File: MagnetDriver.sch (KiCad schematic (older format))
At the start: 54 parts, among them J1 MAGNET1, J2 MAGNET2, J3 INPUT_JACK, J4 PWR_IN, Q1 2N3904, Q2 TIP122, Q3 TIP32A, Q4 2N3904, Q5 TIP122, Q6 TIP32A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

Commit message: checked schematic + footprints
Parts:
- C3, C6: value 0.1uf -> 470pf
- J3: footprint HammerheadAudio:Tayda_3.5mm_stereo_TRS_jack_A-853 -> HammerheadAudio:Tayda_SwitchedStereoJack-PJ-307
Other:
- moved on the sheet: C1, C10, C2, C3, C4, C5, C6, C7, C8, C9, D1, D2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

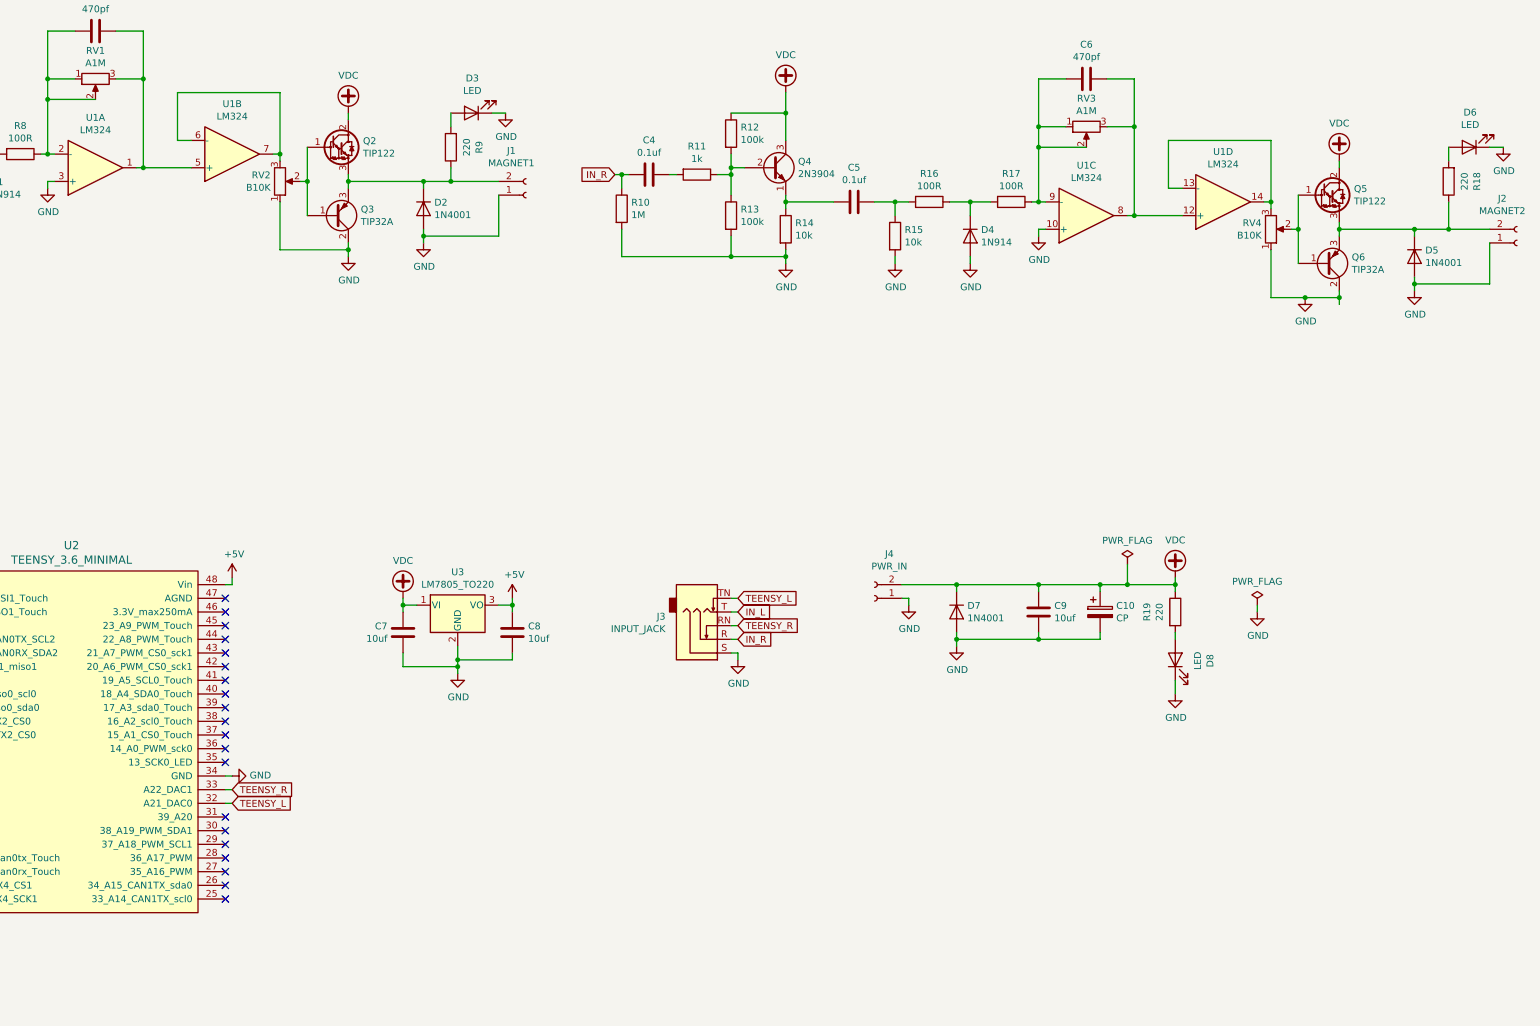
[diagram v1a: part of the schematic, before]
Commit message: arranging components
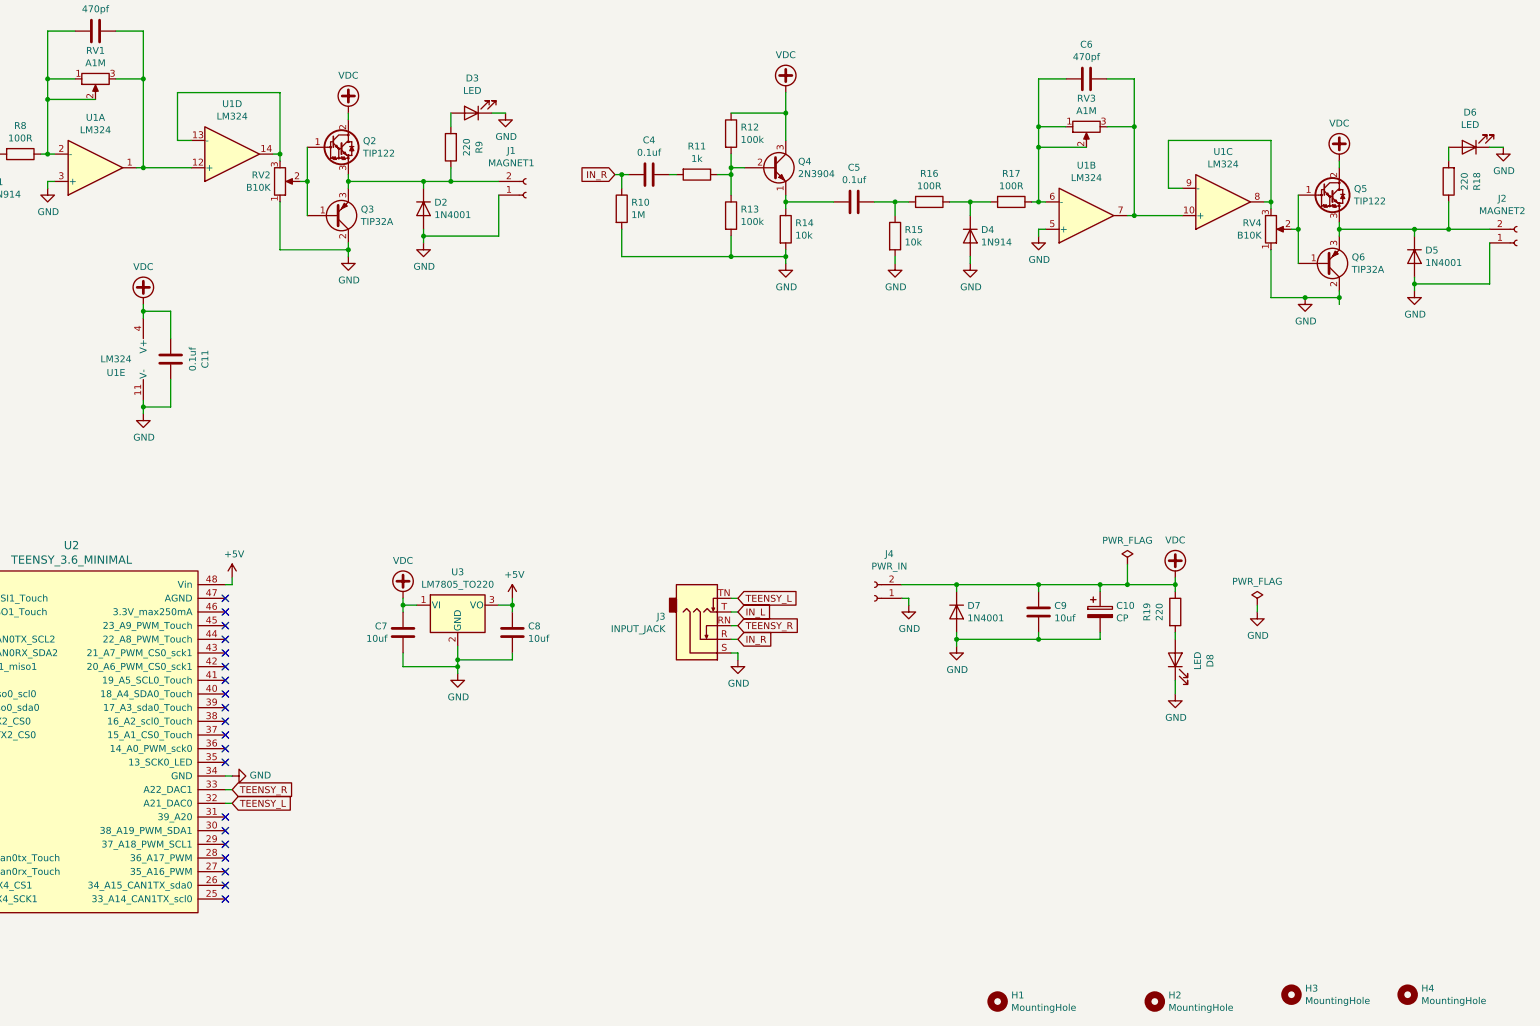
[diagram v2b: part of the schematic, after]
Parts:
- added C11: 0.1uf, Capacitor_THT:C_Disc_D3.0mm_W2.0mm_P2.50mm, symbol Device:C
- added H1, H2, H3, H4: MountingHole, HammerheadAudio:M3_MOUNT_KEEPOUT, symbol Mechanical:MountingHole
- added unit 5 of U1
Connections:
- net GND: now also U1.5 (+), C11.1, U1.11 (V-); no longer U1.10 (+)
- net VDC: now also C11.2, U1.4 (V+)
- net at C3.1, RV1.3, U1.1: now also U1.12 (+); no longer U1.5 (+)
- net at C6.1, RV3.3: now also U1.10 (+), U1.7; no longer U1.12 (+), U1.8
- net at C6.2, R17.1, RV3.1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: now also U1.6 (-); no longer U1.9 (-)
- net at U1.13 (-), U1.14: now also RV2.3; no longer RV4.3
- new net: RV4.3, U1.8, U1.9 (-)
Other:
- moved on the sheet: U1B, U1C, U1D
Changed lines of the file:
@@
 L Amplifier_Operational:LM324 U1
 U 2 1 5FFAB035
-P 5650 2300
-F 0 "U1" H 5650 1933 50  0000 C CNN
-F 1 "LM324" H 5650 2024 50  0000 C CNN
-F 2 "Package_DIP:DIP-14_W7.62mm_Socket" H 5600 2400 50  0001 C CNN
-F 3 "http://www.ti.com/lit/ds/symlink/lm2902-n.pdf" H 5700 2500 50  0001 C CNN
-	2    5650 2300
+P 11900 2750
+F 0 "U1" H 11900 2383 50  0000 C CNN
+F 1 "LM324" H 11900 2474 50  0000 C CNN
+F 2 "Package_DIP:DIP-14_W7.62mm_Socket" H 11850 2850 50  0001 C CNN
+F 3 "http://www.ti.com/lit/ds/symlink/lm2902-n.pdf" H 11950 2950 50  0001 C CNN
+	2    11900 2750
 	1    0    0    1
 $EndComp
@@
 L Amplifier_Operational:LM324 U1
 U 3 1 600153C9
-P 11900 2750
-F 0 "U1" H 11900 2383 50  0000 C CNN
-F 1 "LM324" H 11900 2474 50  0000 C CNN
-F 2 "Package_DIP:DIP-14_W7.62mm_Socket" H 11850 2850 50  0001 C CNN
-F 3 "http://www.ti.com/lit/ds/symlink/lm2902-n.pdf" H 11950 2950 50  0001 C CNN
-	3    11900 2750
+P 12900 2650
+F 0 "U1" H 12900 2283 50  0000 C CNN
+F 1 "LM324" H 12900 2374 50  0000 C CNN
+F 2 "Package_DIP:DIP-14_W7.62mm_Socket" H 12850 2750 50  0001 C CNN
+F 3 "http://www.ti.com/lit/ds/symlink/lm2902-n.pdf" H 12950 2850 50  0001 C CNN
+	3    12900 2650
 	1    0    0    1
 $EndComp
@@
 L Amplifier_Operational:LM324 U1
 U 4 1 60015404
-P 12900 2650
-F 0 "U1" H 12900 2283 50  0000 C CNN
-F 1 "LM324" H 12900 2374 50  0000 C CNN
-F 2 "Package_DIP:DIP-14_W7.62mm_Socket" H 12850 2750 50  0001 C CNN
-F 3 "http://www.ti.com/lit/ds/symlink/lm2902-n.pdf" H 12950 2850 50  0001 C CNN
-	4    12900 2650
+P 5650 2300
+F 0 "U1" H 5650 1933 50  0000 C CNN
+F 1 "LM324" H 5650 2024 50  0000 C CNN
+F 2 "Package_DIP:DIP-14_W7.62mm_Socket" H 5600 2400 50  0001 C CNN
+F 3 "http://www.ti.com/lit/ds/symlink/lm2902-n.pdf" H 5700 2500 50  0001 C CNN
+	4    5650 2300
 	1    0    0    1
 $EndComp
@@
 Wire Wire Line
 	13150 5600 13150 5650
+$Comp
+L Mechanical:MountingHole H1
+U 1 1 605EE444
+P 11250 8500
+F 0 "H1" H 11350 8546 50  0000 L CNN
+F 1 "MountingHole" H 11350 8455 50  0000 L CNN
+F 2 "HammerheadAudio:M3_MOUNT_KEEPOUT" H 11250 8500 50  0001 C CNN
+F 3 "~" H 11250 8500 50  0001 C CNN
+	1    11250 8500
+	1    0    0    -1
+$EndComp
+$Comp
+L Mechanical:MountingHole H2
+U 1 1 605EE643
+P 12400 8500
+F 0 "H2" H 12500 8546 50  0000 L CNN
+F 1 "MountingHole" H 12500 8455 50  0000 L CNN
+F 2 "HammerheadAudio:M3_MOUNT_KEEPOUT" H 12400 8500 50  0001 C CNN
+F 3 "~" H 12400 8500 50  0001 C CNN
+	1    12400 8500
+	1    0    0    -1
+$EndComp
+$Comp
+L Mechanical:MountingHole H3
+U 1 1 605EE8CF
+P 13400 8450
+F 0 "H3" H 13500 8496 50  0000 L CNN
+F 1 "MountingHole" H 13500 8405 50  0000 L CNN
+F 2 "HammerheadAudio:M3_MOUNT_KEEPOUT" H 13400 8450 50  0001 C CNN
+F 3 "~" H 13400 8450 50  0001 C CNN
+	1    13400 8450
+	1    0    0    -1
+$EndComp
+$Comp
+L Mechanical:MountingHole H4
+U 1 1 605EEB7D
+P 14250 8450
+F 0 "H4" H 14350 8496 50  0000 L CNN
+F 1 "MountingHole" H 14350 8405 50  0000 L CNN
+F 2 "HammerheadAudio:M3_MOUNT_KEEPOUT" H 14250 8450 50  0001 C CNN
+F 3 "~" H 14250 8450 50  0001 C CNN
+	1    14250 8450
+	1    0    0    -1
+$EndComp
+$Comp
+L Amplifier_Operational:LM324 U1
+U 5 1 606261BA
+P 4900 3800
+F 0 "U1" H 5000 3700 50  0000 C CNN
+F 1 "LM324" H 5000 3800 50  0000 C CNN
+F 2 "Package_DIP:DIP-14_W7.62mm_Socket" H 4850 3900 50  0001 C CNN
+F 3 "http://www.ti.com/lit/ds/symlink/lm2902-n.pdf" H 4950 4000 50  0001 C CNN
+	5    4900 3800
+	-1   0    0    -1
+$EndComp
+$Comp
+L power:GND #PWR031
+U 1 1 6062685C
+P 5000 4200
+F 0 "#PWR031" H 5000 3950 50  0001 C CNN
+F 1 "GND" H 5005 4027 50  0000 C CNN
+F 2 "" H 5000 4200 50  0001 C CNN
+F 3 "" H 5000 4200 50  0001 C CNN
+	1    5000 4200
+	1    0    0    -1
+$EndComp
+$Comp
+L power:VDC #PWR030
+U 1 1 60640F65
+P 5000 3400
+F 0 "#PWR030" H 5000 3300 50  0001 C CNN
+F 1 "VDC" H 5000 3675 50  0000 C CNN
+F 2 "" H 5000 3400 50  0001 C CNN
+F 3 "" H 5000 3400 50  0001 C CNN
+	1    5000 3400
+	1    0    0    -1
+$EndComp
+Wire Wire Line
+	5000 4100 5000 4150
+Wire Wire Line
+	5000 3400 5000 3450
+$Comp
+L Device:C C11
+U 1 1 6065D093
+P 5200 3800
+F 0 "C11" V 4948 3800 50  0000 C CNN
+F 1 "0.1uf" V 5039 3800 50  0000 C CNN
+F 2 "Capacitor_THT:C_Disc_D3.0mm_W2.0mm_P2.50mm" H 5238 3650 50  0001 C CNN
+F 3 "~" H 5200 3800 50  0001 C CNN
+	1    5200 3800
+	-1   0    0    1
+$EndComp
+Wire Wire Line
+	5000 3450 5200 3450
+Wire Wire Line
+	5200 3450 5200 3650
+Connection ~ 5000 3450
+Wire Wire Line
+	5000 3450 5000 3500
+Wire Wire Line
+	5000 4150 5200 4150
+Wire Wire Line
+	5200 4150 5200 3950
+Connection ~ 5000 4150
+Wire Wire Line
+	5000 4150 5000 4200
 $EndSCHEMATC

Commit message: placed components
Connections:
- net VDC: now also R12.2, R3.2; no longer R12.1, R3.1
- net at Q1.2 (B), R2.1, R4.1: now also R3.1; no longer R3.2
- net at Q4.2 (B), R11.1, R13.1: now also R12.1; no longer R12.2
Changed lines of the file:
@@
 F 3 "~" H 2050 1800 50  0001 C CNN
 	1    2050 1800
-	1    0    0    -1
+	-1   0    0    1
 $EndComp
 $Comp
@@
 F 3 "~" H 9300 2150 50  0001 C CNN
 	1    9300 2150
-	1    0    0    -1
-$EndComp
-$Comp
+	-1   0    0    1
+$EndComp
+$Comp

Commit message: backup before layout changes
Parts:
- removed U3: LM7805_TO220, Package_TO_SOT_THT:TO-220-3_Horizontal_TabDown, symbol Regulator_Linear:LM7805_TO220
- added D9: DNP, LED_THT:LED_D5.0mm, symbol Device:LED
- added Q7: DNP, Package_TO_SOT_THT:TO-92_Inline, symbol Transistor_BJT:2N3904
- added R20, R21, R22: DNP, HammerheadAudio:R_THT_P7.62, symbol Device:R
- added SW1: DNP, HammerheadAudio:Tayda_Slide_SPDT, symbol Switch:SW_SPDT
- added U3: R-78E5.0-0.5, Converter_DCDC:Converter_DCDC_RECOM_R-78E-0.5_THT, symbol Regulator_Switching:R-78E5.0-0.5
- C1, C11, C2, C4, C5: CSV (none) -> C1620173; LCSC (none) -> C1620173
- C3, C6: CSV (none) -> C1620141; LCSC (none) -> C1620141
- C7, C8: value 10uf -> DNP
- C9: CSV (none) -> C2761740; LCSC (none) -> C2761740
- D1, D4: CSV (none) -> C258180; LCSC (none) -> C258180
- D2, D5, D7: CSV (none) -> C2456; LCSC (none) -> C2456
- D3, D6, D8: CSV (none) -> C2895493; LCSC (none) -> C2895493
- J1, J2, J4: CSV (none) -> C430324; LCSC (none) -> C430324
- J3: CSV (none) -> C16684; LCSC (none) -> C16684
- Q1, Q4: CSV (none) -> C2874602; LCSC (none) -> C2874602
- Q2, Q5: CSV (none) -> C16283; LCSC (none) -> C16283
- Q3, Q6: CSV (none) -> C2927632; LCSC (none) -> C2927632
- R11, R2: CSV (none) -> C2894541; LCSC (none) -> C2894541
- R12, R13, R3, R4: CSV (none) -> C714036; LCSC (none) -> C714036
- R14, R15, R5, R6: CSV (none) -> C172967; LCSC (none) -> C172967
- R16, R17, R7, R8: CSV (none) -> C57438; LCSC (none) -> C57438
- R18, R19, R9: value 220 -> 1k; CSV (none) -> C2894541; LCSC (none) -> C2894541
- RV1, RV2, RV3, RV4: CSV (none) -> C5205027; LCSC (none) -> C5205027
- U1: CSV (none) -> C132508; LCSC (none) -> C132508
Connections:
- net +5V: now also SW1.2 (B), U3.3 (OUT); no longer U2.48 (Vin)
- net GND: now also D9.1 (K), Q7.1 (E), R22.1, U3.2 (GND)
- net VDC: now also U3.1 (IN)
- net at U2.44 (22_A8_PWM_Touch): now also Q7.3 (C)
- net at U2.45 (23_A9_PWM_Touch): now also R20.2
- new net: SW1.3 (C), U2.48 (Vin)
- new net: R21.2, SW1.1 (A)
- new net: D9.2 (A), R20.1
- new net: Q7.2 (B), R21.1, R22.2
- no-connect marks 43 -> 41
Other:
- moved on the sheet: C10, C7, C8, C9, D7, D8, H1, H2, H3, H4, J3, J4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
